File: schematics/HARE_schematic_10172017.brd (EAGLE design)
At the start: 105.1 x 80 mm, 87 parts, among them IC1 NE5532N, IC2 NE5532N, IC3 FT232RL, IC4 NE5532N, IC5 7805DT, J2 STEREOSW, J3 STEREOSW, Q1 16 MHz, SW1 3PDTBLUE, SW2 Reset Button, U1 ATMEGA328P-PU, X2 USB-B-H

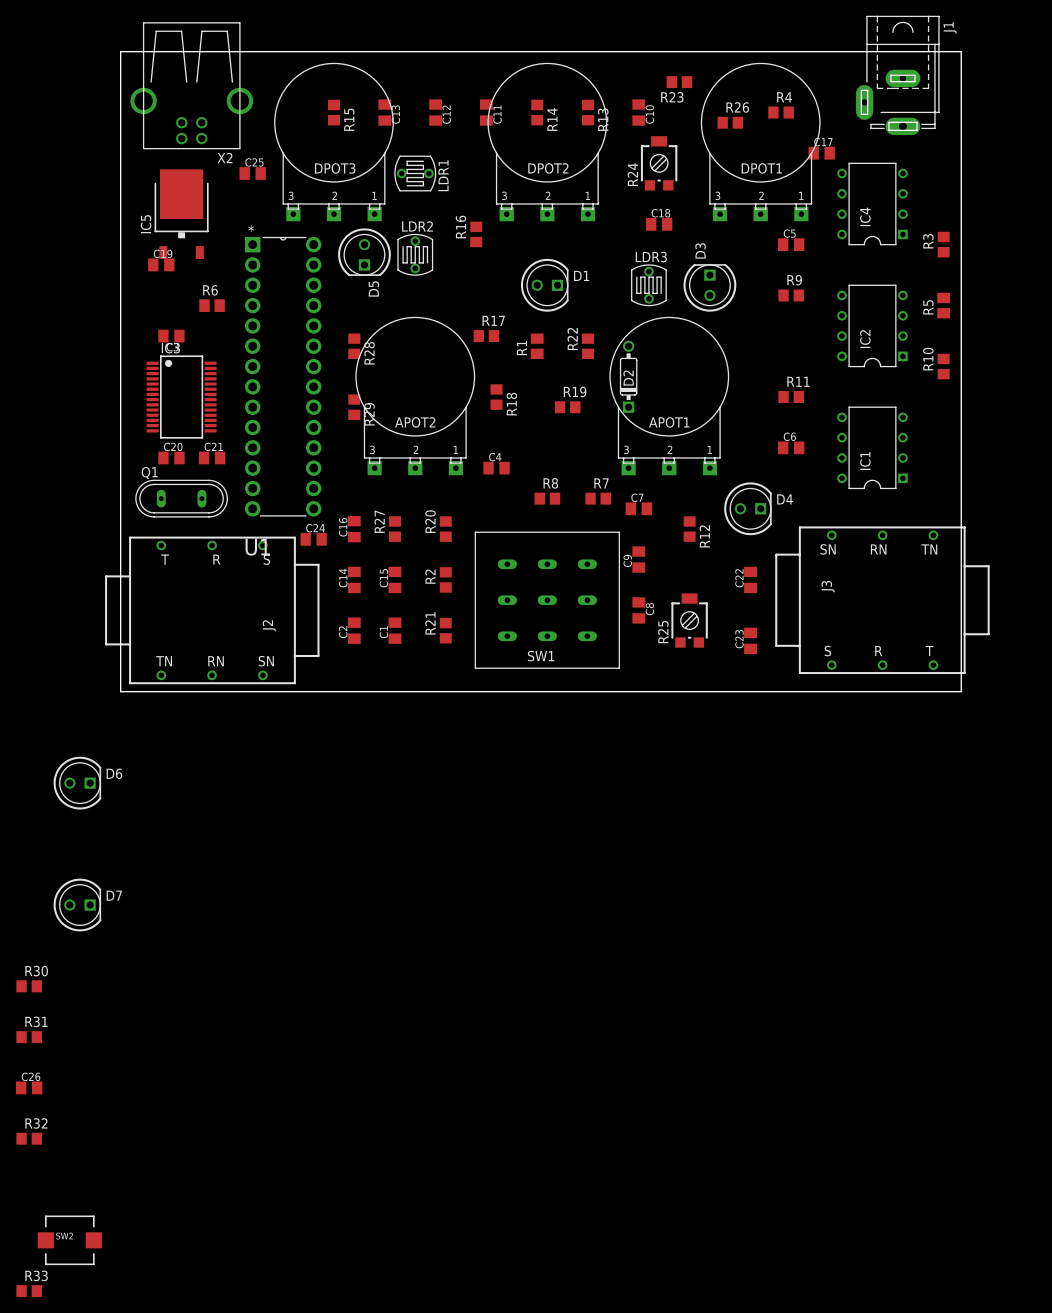
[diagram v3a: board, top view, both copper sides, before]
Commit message: Connected FT232 to reset switch.
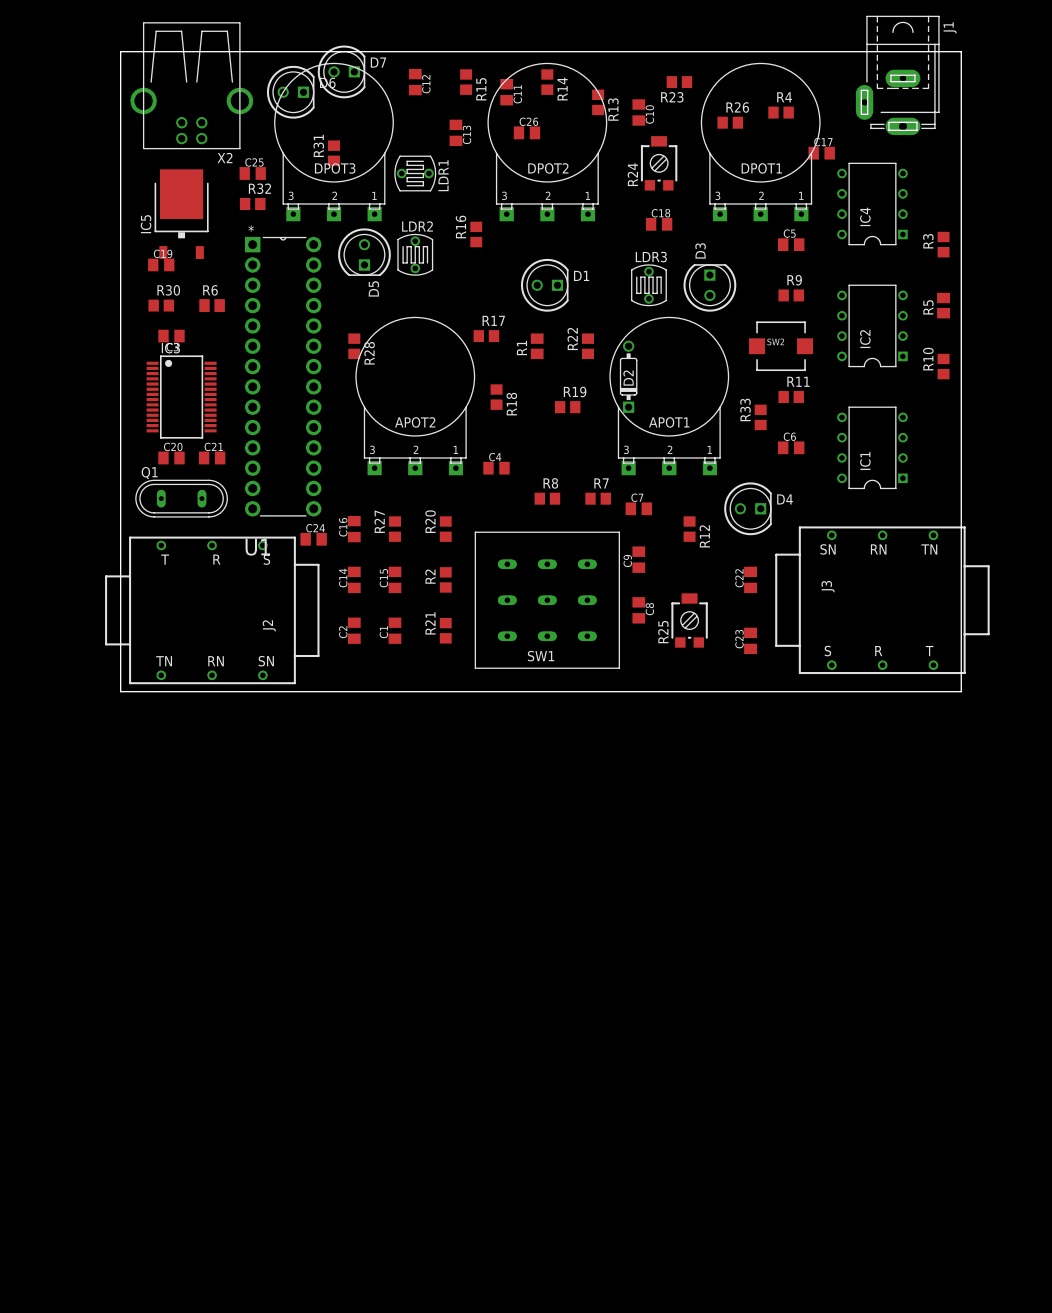
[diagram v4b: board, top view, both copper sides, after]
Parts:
- removed R29: 10k, resistor:R0805
- moved SW2 142.8 mm to (82.5, 43.2)
- moved R33 142.4 mm to (80.0, 34.3), turned to 90 degrees
- moved C26 134.6 mm to (50.8, 69.8)
- moved R32 120.1 mm to (16.5, 61.0)
- moved R31 116.9 mm to (26.7, 67.3), turned to 90 degrees
- moved D7 109.2 mm to (27.9, 77.5)
- moved D6 90.4 mm to (21.6, 74.9)
- moved R30 86.7 mm to (5.08, 48.3)
- moved R15 16.9 mm to (43.2, 76.2)
- moved C13 9.25 mm to (41.9, 69.8)
- moved C12 4.58 mm to (36.8, 76.2)
- moved R14 4.02 mm to (53.3, 76.2)
- moved C11 3.59 mm to (48.3, 74.9)
- moved R13 1.80 mm to (59.7, 73.7)
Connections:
- net 5V: no longer R29.1
- net N$62: no longer R29.2
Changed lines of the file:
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@@
 <element name="LDR2" library="gm-resistors" package="LDR338-54C" value="" x="36.83" y="54.61"/>
 <element name="C10" library="resistor" package="C0805K" value="1uF" x="64.77" y="72.39" rot="R270"/>
-<element name="R13" library="resistor" package="R0805" value="47k" x="58.42" y="72.39" rot="R270"/>
-<element name="R14" library="resistor" package="R0805" value="100k" x="52.07" y="72.39" rot="R270"/>
-<element name="C11" library="resistor" package="C0805K" value="0.22uF" x="45.72" y="72.39" rot="R270"/>
-<element name="C12" library="resistor" package="C0805K" value="0.22uF" x="39.37" y="72.39" rot="R270"/>
-<element name="C13" library="resistor" package="C0805K" value="1uF" x="33.02" y="72.39" rot="R270"/>
-<element name="R15" library="resistor" package="R0805" value="10k" x="26.67" y="72.39" rot="R270"/>
+<element name="R13" library="resistor" package="R0805" value="47k" x="59.69" y="73.66" rot="R270"/>
+<element name="R14" library="resistor" package="R0805" value="100k" x="53.34" y="76.2" rot="R270"/>
+<element name="C11" library="resistor" package="C0805K" value="0.22uF" x="48.26" y="74.93" rot="R270"/>
+<element name="C12" library="resistor" package="C0805K" value="0.22uF" x="36.83" y="76.2" rot="R270"/>
+<element name="C13" library="resistor" package="C0805K" value="1uF" x="41.91" y="69.85" rot="R270"/>
+<element name="R15" library="resistor" package="R0805" value="10k" x="43.18" y="76.2" rot="R270"/>
 <element name="D2" library="gm-diodes" package="DO35-3" value="1N4148-3" x="63.5" y="39.37" rot="R90"/>
 <element name="R16" library="resistor" package="R0805" value="1k" x="44.45" y="57.15" rot="R90"/>
@@
 <element name="R27" library="resistor" package="R0805" value="1k" x="34.29" y="20.32" rot="R90"/>
 <element name="R28" library="resistor" package="R0805" value="1k" x="29.21" y="43.18" rot="R270"/>
-<element name="R29" library="resistor" package="R0805" value="10k" x="29.21" y="35.56" rot="R270"/>
-<element name="D6" library="gm-diodes" package="LED5MM" value="LED5MM" x="-5.08" y="-11.43"/>
-<element name="D7" library="gm-diodes" package="LED5MM" value="LED5MM" x="-5.08" y="-26.67"/>
-<element name="R30" library="resistor" package="R0805" value="1k" x="-11.43" y="-36.83"/>
-<element name="R31" library="resistor" package="R0805" value="1k" x="-11.43" y="-43.18"/>
-<element name="C26" library="resistor" package="C0805K" value="100nF" x="-11.43" y="-49.53"/>
-<element name="R32" library="resistor" package="R0805" value="1k" x="-11.43" y="-55.88"/>
-<element name="SW2" library="adafruit" package="PUSHBUTTON_SMD_SJ" value="Reset Button" x="-6.35" y="-68.58"/>
-<element name="R33" library="resistor" package="R0805" value="10k" x="-11.43" y="-74.93"/>
+<element name="D6" library="gm-diodes" package="LED5MM" value="LED5MM" x="21.59" y="74.93"/>
+<element name="D7" library="gm-diodes" package="LED5MM" value="LED5MM" x="27.94" y="77.47"/>
+<element name="R30" library="resistor" package="R0805" value="1k" x="5.08" y="48.26"/>
+<element name="R31" library="resistor" package="R0805" value="1k" x="26.67" y="67.31" rot="R90"/>
+<element name="C26" library="resistor" package="C0805K" value="100nF" x="50.8" y="69.85"/>
+<element name="R32" library="resistor" package="R0805" value="1k" x="16.51" y="60.96"/>
+<element name="SW2" library="adafruit" package="PUSHBUTTON_SMD_SJ" value="Reset Button" x="82.55" y="43.18"/>
+<element name="R33" library="resistor" package="R0805" value="10k" x="80.01" y="34.29" rot="R90"/>
 </elements>
 <signals>
@@
 <wire x1="17.78" y1="2.045" x2="17.78" y2="18.275" width="0" layer="19" extent="1-1"/>
 <wire x1="11.43" y1="2.045" x2="17.78" y2="2.045" width="0" layer="19" extent="1-1"/>
-<wire x1="-12.43" y1="-49.53" x2="11.43" y2="2.045" width="0" layer="19" extent="1-1"/>
-<wire x1="-3.35" y1="-68.58" x2="-12.43" y2="-49.53" width="0" layer="19" extent="1-1"/>
+<wire x1="49.8" y1="69.85" x2="11.43" y2="2.045" width="0" layer="19" extent="1-1"/>
+<wire x1="85.55" y1="43.18" x2="49.8" y2="69.85" width="0" layer="19" extent="1-1"/>
 </signal>
 <signal name="INPUT">
@@
 <contactref element="C10" pad="1"/>
 <contactref element="R13" pad="1"/>
-<wire x1="64.77" y1="73.39" x2="58.42" y2="73.34" width="0" layer="19" extent="1-1"/>
+<wire x1="64.77" y1="73.39" x2="59.69" y2="74.61" width="0" layer="19" extent="1-1"/>
 </signal>
 <signal name="N$22">
@@
 <contactref element="C11" pad="2"/>
 <contactref element="IC2" pad="2"/>
-<wire x1="52.07" y1="73.34" x2="45.72" y2="71.39" width="0" layer="19" extent="1-1"/>
-<wire x1="58.42" y1="71.44" x2="52.07" y2="73.34" width="0" layer="19" extent="1-1"/>
-<wire x1="97.79" y1="44.45" x2="58.42" y2="71.44" width="0" layer="19" extent="1-1"/>
+<wire x1="53.34" y1="77.15" x2="48.26" y2="73.93" width="0" layer="19" extent="1-1"/>
+<wire x1="59.69" y1="72.71" x2="53.34" y2="77.15" width="0" layer="19" extent="1-1"/>
+<wire x1="97.79" y1="44.45" x2="59.69" y2="72.71" width="0" layer="19" extent="1-1"/>
 </signal>
 <signal name="N$23">
@@
 <contactref element="R15" pad="2"/>
 <contactref element="C13" pad="2"/>
-<wire x1="33.02" y1="71.39" x2="26.67" y2="71.44" width="0" layer="19" extent="1-1"/>
-<wire x1="52.07" y1="71.44" x2="33.02" y2="71.39" width="0" layer="19" extent="1-1"/>
-<wire x1="36.83" y1="52.9082" x2="52.07" y2="71.44" width="0" layer="19" extent="1-1"/>
+<wire x1="41.91" y1="68.85" x2="43.18" y2="75.25" width="0" layer="19" extent="1-1"/>
+<wire x1="53.34" y1="75.25" x2="41.91" y2="68.85" width="0" layer="19" extent="1-1"/>
+<wire x1="36.83" y1="52.9082" x2="53.34" y2="75.25" width="0" layer="19" extent="1-1"/>
 <wire x1="97.79" y1="41.91" x2="36.83" y2="52.9082" width="0" layer="19" extent="1-1"/>
 </signal>
@@
 <contactref element="LDR2" pad="1"/>
 <contactref element="R15" pad="1"/>
-<wire x1="39.37" y1="73.39" x2="26.67" y2="73.34" width="0" layer="19" extent="1-1"/>
-<wire x1="36.83" y1="56.3118" x2="39.37" y2="73.39" width="0" layer="19" extent="1-1"/>
+<wire x1="36.83" y1="77.2" x2="43.18" y2="77.15" width="0" layer="19" extent="1-1"/>
+<wire x1="36.83" y1="56.3118" x2="36.83" y2="77.2" width="0" layer="19" extent="1-1"/>
 </signal>
 <signal name="N$27">
@@
 <contactref element="D2" pad="A"/>
 <wire x1="63.5" y1="43.18" x2="44.45" y2="58.1" width="0" layer="19" extent="1-1"/>
-<wire x1="39.37" y1="71.39" x2="63.5" y2="43.18" width="0" layer="19" extent="1-1"/>
-<wire x1="45.72" y1="73.39" x2="39.37" y2="71.39" width="0" layer="19" extent="1-1"/>
+<wire x1="36.83" y1="75.2" x2="63.5" y2="43.18" width="0" layer="19" extent="1-1"/>
+<wire x1="48.26" y1="75.93" x2="36.83" y2="75.2" width="0" layer="19" extent="1-1"/>
 </signal>
 <signal name="N$24">
@@
 <contactref element="DPOT1" pad="3"/>
 <contactref element="IC3" pad="20"/>
-<contactref element="R29" pad="1"/>
 <contactref element="X2" pad="VBUS"/>
 <contactref element="C26" pad="2"/>
@@
 <wire x1="11.245" y1="35.855" x2="16.51" y2="40.64" width="0" layer="19" extent="1-1"/>
 <wire x1="24.13" y1="35.56" x2="16.51" y2="40.64" width="0" layer="19" extent="1-1"/>
-<wire x1="29.21" y1="36.51" x2="24.13" y2="35.56" width="0" layer="19" extent="1-1"/>
 <wire x1="78.74" y1="14.97" x2="74.93" y2="59.69" width="0" layer="19" extent="1-1"/>
 <wire x1="78.74" y1="7.35" x2="78.74" y2="14.97" width="0" layer="19" extent="1-1"/>
-<wire x1="-10.43" y1="-49.53" x2="11.245" y2="35.855" width="0" layer="19" extent="1-1"/>
-<wire x1="-12.38" y1="-74.93" x2="-10.43" y2="-49.53" width="0" layer="19" extent="1-1"/>
+<wire x1="51.8" y1="69.85" x2="11.245" y2="35.855" width="0" layer="19" extent="1-1"/>
+<wire x1="80.01" y1="33.34" x2="51.8" y2="69.85" width="0" layer="19" extent="1-1"/>
 </signal>
 <signal name="VCA_IN">
@@
 <signal name="N$62">
 <contactref element="IC3" pad="19"/>
-<contactref element="R29" pad="2"/>
-<wire x1="29.21" y1="34.61" x2="11.245" y2="35.205" width="0" layer="19" extent="1-1"/>
 </signal>
 <signal name="N$63">
 <contactref element="D6" pad="A"/>
 <contactref element="R30" pad="2"/>
-<wire x1="-6.35" y1="-11.43" x2="-10.48" y2="-36.83" width="0" layer="19" extent="1-1"/>
+<wire x1="20.32" y1="74.93" x2="6.03" y2="48.26" width="0" layer="19" extent="1-1"/>
 </signal>
 <signal name="N$64">
 <contactref element="D7" pad="A"/>
 <contactref element="R31" pad="2"/>
-<wire x1="-6.35" y1="-26.67" x2="-10.48" y2="-43.18" width="0" layer="19" extent="1-1"/>
+<wire x1="26.67" y1="77.47" x2="26.67" y2="68.26" width="0" layer="19" extent="1-1"/>
 </signal>
 <signal name="VCCIO">
 <contactref element="R31" pad="1"/>
 <contactref element="R30" pad="1"/>
-<wire x1="-12.38" y1="-36.83" x2="-12.38" y2="-43.18" width="0" layer="19" extent="1-1"/>
+<wire x1="4.13" y1="48.26" x2="26.67" y2="66.36" width="0" layer="19" extent="1-1"/>
 </signal>
 <signal name="CBUS1">
@@
 <contactref element="SW2" pad="P$2"/>
 <contactref element="R33" pad="2"/>
-<wire x1="-9.35" y1="-68.58" x2="-10.48" y2="-74.93" width="0" layer="19" extent="1-1"/>
-<wire x1="-12.38" y1="-55.88" x2="-9.35" y2="-68.58" width="0" layer="19" extent="1-1"/>
-<wire x1="16.51" y1="55.88" x2="-12.38" y2="-55.88" width="0" layer="19" extent="1-1"/>
+<wire x1="79.55" y1="43.18" x2="80.01" y2="35.24" width="0" layer="19" extent="1-1"/>
+<wire x1="15.56" y1="60.96" x2="79.55" y2="43.18" width="0" layer="19" extent="1-1"/>
+<wire x1="16.51" y1="55.88" x2="15.56" y2="60.96" width="0" layer="19" extent="1-1"/>
 </signal>
 <signal name="RTS#">
 <contactref element="IC3" pad="3"/>
 <contactref element="R32" pad="2"/>
-<wire x1="3.995" y1="39.755" x2="-10.48" y2="-55.88" width="0" layer="19" extent="1-1"/>
+<wire x1="3.995" y1="39.755" x2="17.46" y2="60.96" width="0" layer="19" extent="1-1"/>
 </signal>
 <signal name="CTS#">
